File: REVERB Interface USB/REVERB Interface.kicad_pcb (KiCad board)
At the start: 2 copper layers, 90.2 x 95.9 mm, 61 parts, among them J1 RPiZeroW, J2 Iridium, J3 APRS, J4 Antenna, J6 USB_B_Micro, J7 USB, J8 USBPOGO, M1 MountingHole_Pad, M2 MountingHole_Pad, M3 MountingHole_Pad, M4 MountingHole_Pad, M5 PiMount, M6 PiMount, M7 PiMount, M8 PiMount, U1 LSM9DS1BOB, U2 MAX3232, U3 CY7C65213-28PVXI, U4 TXB0104D

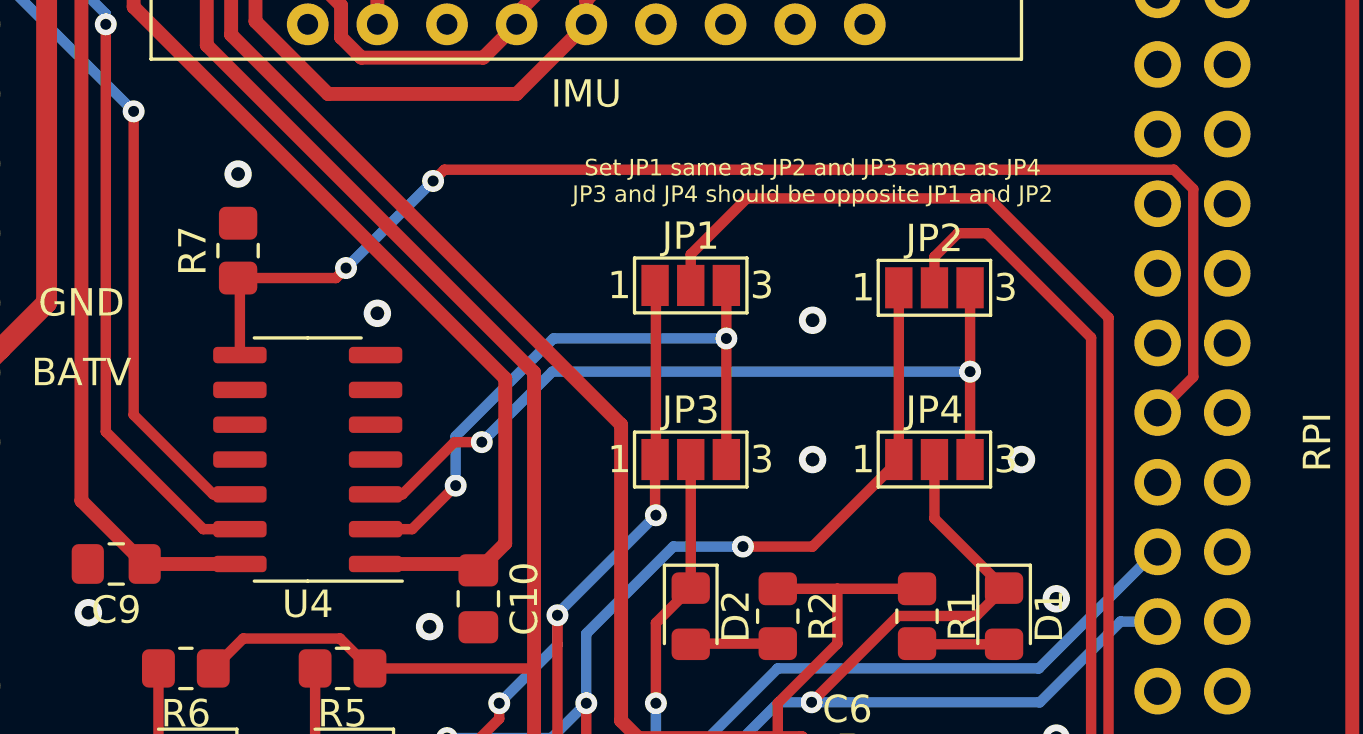
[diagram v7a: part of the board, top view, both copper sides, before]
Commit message: tie OE high
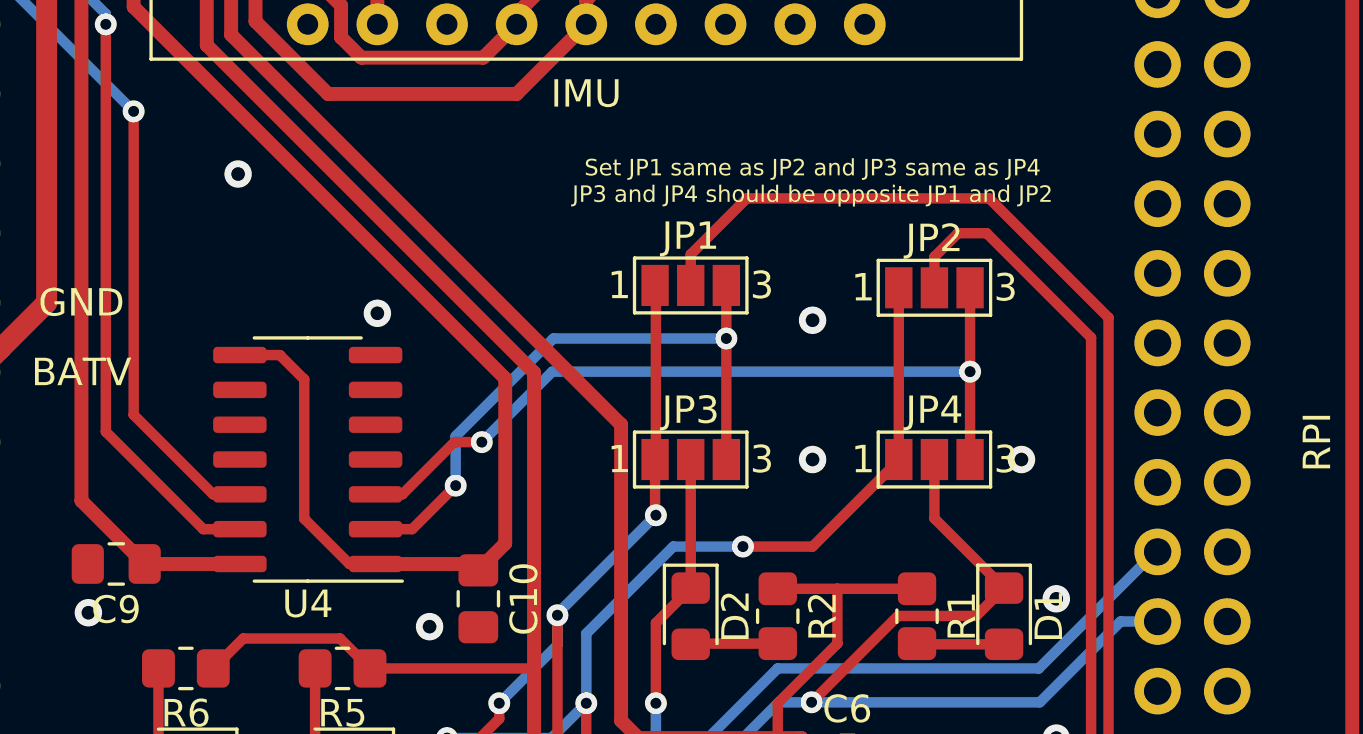
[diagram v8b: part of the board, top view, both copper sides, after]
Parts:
- removed R7: 10K, Resistor_SMD:R_0805_2012Metric_Pad1.20x1.40mm_HandSolder
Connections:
- J1 pad 22: /OE -> (no net)
- U4 pad 8: /OE -> +3V3
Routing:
- net /OE: track 48.3 -> 0.00 mm, vias 2 -> 0
- net +3V3: track 84.1 -> 95.2 mm
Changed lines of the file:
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@@
     (thickness 1.6)
     (drawings 72)
-    (tracks 476)
+    (tracks 469)
     (zones 0)
-    (modules 61)
-    (nets 48)
+    (modules 60)
+    (nets 47)
   )
   (page A4)
@@
   (net 43 "Net-(D12-Pad2)")
   (net 44 /SW10)
-  (net 45 /OE)
-  (net 46 /APRSTXSh)
-  (net 47 /APRSRXSh)
+  (net 45 /APRSTXSh)
+  (net 46 /APRSRXSh)
   (net_class Default "This is the default net class."
     (clearance 0.2)
@@
     (add_net /HWRX)
     (add_net /HWTX)
-    (add_net /OE)
     (add_net /PCM_IN)
     (add_net /R1IN)
@@
       (net 15 +5V))
     (pad 13 smd roundrect (at 2.475 -2.54 180) (size 1.95 0.6) (layers F.Cu F.Paste F.Mask) (roundrect_rratio 0.25)
-      (net 47 /APRSRXSh))
+      (net 46 /APRSRXSh))
     (pad 12 smd roundrect (at 2.475 -1.27 180) (size 1.95 0.6) (layers F.Cu F.Paste F.Mask) (roundrect_rratio 0.25)
-      (net 46 /APRSTXSh))
+      (net 45 /APRSTXSh))
     (pad 11 smd roundrect (at 2.475 0 180) (size 1.95 0.6) (layers F.Cu F.Paste F.Mask) (roundrect_rratio 0.25))
     (pad 10 smd roundrect (at 2.475 1.27 180) (size 1.95 0.6) (layers F.Cu F.Paste F.Mask) (roundrect_rratio 0.25))
     (pad 9 smd roundrect (at 2.475 2.54 180) (size 1.95 0.6) (layers F.Cu F.Paste F.Mask) (roundrect_rratio 0.25))
     (pad 8 smd roundrect (at 2.475 3.81 180) (size 1.95 0.6) (layers F.Cu F.Paste F.Mask) (roundrect_rratio 0.25)
-      (net 45 /OE))
+      (net 14 +3V3))
     (pad 7 smd roundrect (at -2.475 3.81 180) (size 1.95 0.6) (layers F.Cu F.Paste F.Mask) (roundrect_rratio 0.25)
       (net 6 GND))
@@
     )
   )
-  (module Resistor_SMD:R_0805_2012Metric_Pad1.20x1.40mm_HandSolder (layer F.Cu)
-    (at 132.715 100.965 90)
-    (descr "Resistor SMD 0805 (2012 Metric), square (rectangular) end terminal, IPC_7351 nominal with elongated pad for handsoldering. (Body size source: IPC-SM-782 page 72, https://www.pcb-3d.com/wordpress/wp-content/uploads/ipc-sm-782a_amendment_1_and_2.pdf), generated with kicad-footprint-generator")
-    (tags "resistor handsolder")
-    (attr smd)
-    (fp_text reference R7 (at 0 -1.65 90) (layer F.SilkS)
-      (effects (font (size 1 1) (thickness 0.15)))
-    )
-    (fp_text value 10K (at 0 1.65 90) (layer F.Fab)
-      (effects (font (size 1 1) (thickness 0.15)))
-    )
-    (fp_line (start 1.85 0.95) (end -1.85 0.95) (layer F.CrtYd) (width 0.05))
-    (fp_line (start 1.85 -0.95) (end 1.85 0.95) (layer F.CrtYd) (width 0.05))
-    (fp_line (start -1.85 -0.95) (end 1.85 -0.95) (layer F.CrtYd) (width 0.05))
-    (fp_line (start -1.85 0.95) (end -1.85 -0.95) (layer F.CrtYd) (width 0.05))
-    (fp_line (start -0.227064 0.735) (end 0.227064 0.735) (layer F.SilkS) (width 0.12))
-    (fp_line (start -0.227064 -0.735) (end 0.227064 -0.735) (layer F.SilkS) (width 0.12))
-    (fp_line (start 1 0.625) (end -1 0.625) (layer F.Fab) (width 0.1))
-    (fp_line (start 1 -0.625) (end 1 0.625) (layer F.Fab) (width 0.1))
-    (fp_line (start -1 -0.625) (end 1 -0.625) (layer F.Fab) (width 0.1))
-    (fp_line (start -1 0.625) (end -1 -0.625) (layer F.Fab) (width 0.1))
-    (fp_text user %R (at 0 0 90) (layer F.Fab)
-      (effects (font (size 0.5 0.5) (thickness 0.08)))
-    )
-    (pad 2 smd roundrect (at 1 0 90) (size 1.2 1.4) (layers F.Cu F.Paste F.Mask) (roundrect_rratio 0.2083325)
-      (net 6 GND))
-    (pad 1 smd roundrect (at -1 0 90) (size 1.2 1.4) (layers F.Cu F.Paste F.Mask) (roundrect_rratio 0.2083325)
-      (net 45 /OE))
-    (model ${KISYS3DMOD}/Resistor_SMD.3dshapes/R_0805_2012Metric.wrl
-      (at (xyz 0 0 0))
-      (scale (xyz 1 1 1))
-      (rotate (xyz 0 0 0))
-    )
-  )
   (module Capacitor_SMD:C_0805_2012Metric_Pad1.18x1.45mm_HandSolder (layer F.Cu)
     (at 141.478 113.665 270)
@@
     (pad 7 thru_hole oval (at 0 -7.62 180) (size 1.7 1.7) (drill 1) (layers *.Cu *.Mask))
     (pad 6 thru_hole oval (at -2.54 -5.08 180) (size 1.7 1.7) (drill 1) (layers *.Cu *.Mask)
-      (net 46 /APRSTXSh))
+      (net 45 /APRSTXSh))
     (pad 5 thru_hole oval (at 0 -5.08 180) (size 1.7 1.7) (drill 1) (layers *.Cu *.Mask))
     (pad 4 thru_hole oval (at -2.54 -2.54 180) (size 1.7 1.7) (drill 1) (layers *.Cu *.Mask)
-      (net 47 /APRSRXSh))
+      (net 46 /APRSRXSh))
     (pad 3 thru_hole oval (at 0 -2.54 180) (size 1.7 1.7) (drill 1) (layers *.Cu *.Mask))
     (pad 2 thru_hole oval (at -2.54 0 180) (size 1.7 1.7) (drill 1) (layers *.Cu *.Mask))
@@
     (pad 24 thru_hole oval (at -2.54 -27.94) (size 1.7 1.7) (drill 1) (layers *.Cu *.Mask))
     (pad 23 thru_hole oval (at 0 -27.94) (size 1.7 1.7) (drill 1) (layers *.Cu *.Mask))
-    (pad 22 thru_hole oval (at -2.54 -25.4) (size 1.7 1.7) (drill 1) (layers *.Cu *.Mask)
-      (net 45 /OE))
+    (pad 22 thru_hole oval (at -2.54 -25.4) (size 1.7 1.7) (drill 1) (layers *.Cu *.Mask))
     (pad 21 thru_hole oval (at 0 -25.4) (size 1.7 1.7) (drill 1) (layers *.Cu *.Mask))
     (pad 20 thru_hole oval (at -2.54 -22.86) (size 1.7 1.7) (drill 1) (layers *.Cu *.Mask)
@@
   (gr_line (start 106.836 80.799) (end 108.741 82.704) (layer Edge.Cuts) (width 0.05))
   (gr_line (start 106.836 52.859) (end 106.836 80.799) (layer Edge.Cuts) (width 0.05))
+  (segment (start 136.652 101.6) (end 136.652 101.6) (width 0.381) (layer B.Cu) (net 0))
   (segment (start 133.397499 126.5975) (end 134.434999 127.635) (width 0.508) (layer F.Cu) (net 1))
   (segment (start 130.81 126.5975) (end 133.397499 126.5975) (width 0.508) (layer F.Cu) (net 1))
@@
   (segment (start 142.459001 111.646499) (end 142.459001 105.629001) (width 0.508) (layer F.Cu) (net 14))
   (segment (start 141.478 112.6275) (end 142.459001 111.646499) (width 0.508) (layer F.Cu) (net 14))
+  (segment (start 136.779 112.395) (end 137.73 112.395) (width 0.381) (layer F.Cu) (net 14))
+  (segment (start 135.128 110.744) (end 136.779 112.395) (width 0.381) (layer F.Cu) (net 14))
+  (segment (start 135.128 105.664) (end 135.128 110.744) (width 0.381) (layer F.Cu) (net 14))
+  (segment (start 134.239 104.775) (end 135.128 105.664) (width 0.381) (layer F.Cu) (net 14))
+  (segment (start 132.78 104.775) (end 134.239 104.775) (width 0.381) (layer F.Cu) (net 14))
   (segment (start 166.256 129.734) (end 166.256 132.274) (width 0.508) (layer F.Cu) (net 15))
   (segment (start 151.286 57.939) (end 151.286 60.479) (width 0.508) (layer F.Cu) (net 15))
@@
   (segment (start 132.461 81.264) (end 132.461 93.091) (width 0.508) (layer F.Cu) (net 44))
   (segment (start 140.065 73.66) (end 132.461 81.264) (width 0.508) (layer F.Cu) (net 44))
-  (segment (start 132.78 102.03) (end 132.715 101.965) (width 0.381) (layer F.Cu) (net 45))
-  (segment (start 132.78 104.775) (end 132.78 102.03) (width 0.381) (layer F.Cu) (net 45))
-  (segment (start 136.652 101.6) (end 136.652 101.6) (width 0.381) (layer B.Cu) (net 45))
-  (via (at 136.652 101.6) (size 0.8) (drill 0.4) (layers F.Cu B.Cu) (net 45))
-  (segment (start 136.287 101.965) (end 136.652 101.6) (width 0.381) (layer F.Cu) (net 45))
-  (segment (start 132.715 101.965) (end 136.287 101.965) (width 0.381) (layer F.Cu) (net 45))
-  (segment (start 166.851441 98.013499) (end 140.238501 98.013499) (width 0.381) (layer F.Cu) (net 45))
-  (segment (start 167.555499 98.717557) (end 166.851441 98.013499) (width 0.381) (layer F.Cu) (net 45))
-  (segment (start 140.238501 98.013499) (end 139.827 98.425) (width 0.381) (layer F.Cu) (net 45))
-  (segment (start 167.555499 105.574501) (end 167.555499 98.717557) (width 0.381) (layer F.Cu) (net 45))
-  (segment (start 166.256 106.874) (end 167.555499 105.574501) (width 0.381) (layer F.Cu) (net 45))
-  (segment (start 136.652 101.6) (end 139.827 98.425) (width 0.381) (layer B.Cu) (net 45))
-  (via (at 139.827 98.425) (size 0.8) (drill 0.4) (layers F.Cu B.Cu) (net 45))
-  (segment (start 128.905 106.955) (end 128.905 95.885) (width 0.381) (layer F.Cu) (net 46))
-  (segment (start 132.78 109.855) (end 131.805 109.855) (width 0.381) (layer F.Cu) (net 46))
-  (segment (start 123.19 90.17) (end 128.905 95.885) (width 0.381) (layer B.Cu) (net 46))
-  (segment (start 131.805 109.855) (end 128.905 106.955) (width 0.381) (layer F.Cu) (net 46))
-  (via (at 128.905 95.885) (size 0.8) (drill 0.4) (layers F.Cu B.Cu) (net 46))
-  (via (at 127.889008 92.71) (size 0.8) (drill 0.4) (layers F.Cu B.Cu) (net 47))
-  (segment (start 127.889008 107.569008) (end 127.889008 92.71) (width 0.381) (layer F.Cu) (net 47))
-  (segment (start 127.889008 92.329008) (end 127.889008 92.71) (width 0.381) (layer B.Cu) (net 47))
-  (segment (start 123.19 87.63) (end 127.889008 92.329008) (width 0.381) (layer B.Cu) (net 47))
-  (segment (start 132.78 111.125) (end 131.445 111.125) (width 0.381) (layer F.Cu) (net 47))
-  (segment (start 131.445 111.125) (end 127.889008 107.569008) (width 0.381) (layer F.Cu) (net 47))
+  (segment (start 128.905 106.955) (end 128.905 95.885) (width 0.381) (layer F.Cu) (net 45))
+  (segment (start 132.78 109.855) (end 131.805 109.855) (width 0.381) (layer F.Cu) (net 45))
+  (segment (start 123.19 90.17) (end 128.905 95.885) (width 0.381) (layer B.Cu) (net 45))
+  (segment (start 131.805 109.855) (end 128.905 106.955) (width 0.381) (layer F.Cu) (net 45))
+  (via (at 128.905 95.885) (size 0.8) (drill 0.4) (layers F.Cu B.Cu) (net 45))
+  (via (at 127.889008 92.71) (size 0.8) (drill 0.4) (layers F.Cu B.Cu) (net 46))
+  (segment (start 127.889008 107.569008) (end 127.889008 92.71) (width 0.381) (layer F.Cu) (net 46))
+  (segment (start 127.889008 92.329008) (end 127.889008 92.71) (width 0.381) (layer B.Cu) (net 46))
+  (segment (start 123.19 87.63) (end 127.889008 92.329008) (width 0.381) (layer B.Cu) (net 46))
+  (segment (start 132.78 111.125) (end 131.445 111.125) (width 0.381) (layer F.Cu) (net 46))
+  (segment (start 131.445 111.125) (end 127.889008 107.569008) (width 0.381) (layer F.Cu) (net 46))
   (zone (net 6) (net_name GND) (layer F.Cu) (hatch edge 0.508)
     (connect_pads (clearance 0.508))
